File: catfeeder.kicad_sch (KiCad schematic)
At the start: 81 parts, among them J1 Barrel_Jack_Switch, J2 USB_B_Mini, J3 RFID, J4 DoorOpen, J5 Scale, J6 Auger Motor, J7 Door Motor, J8 DoorClose, Q1 UMH3N, Q3 MMBT4403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

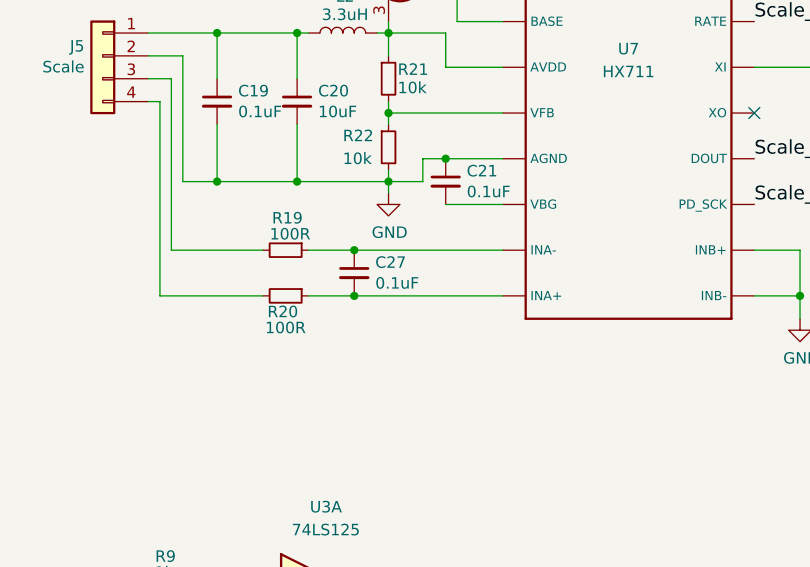
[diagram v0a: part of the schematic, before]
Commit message: Save with new KiCAD version. Cleanup some tracks and vias.
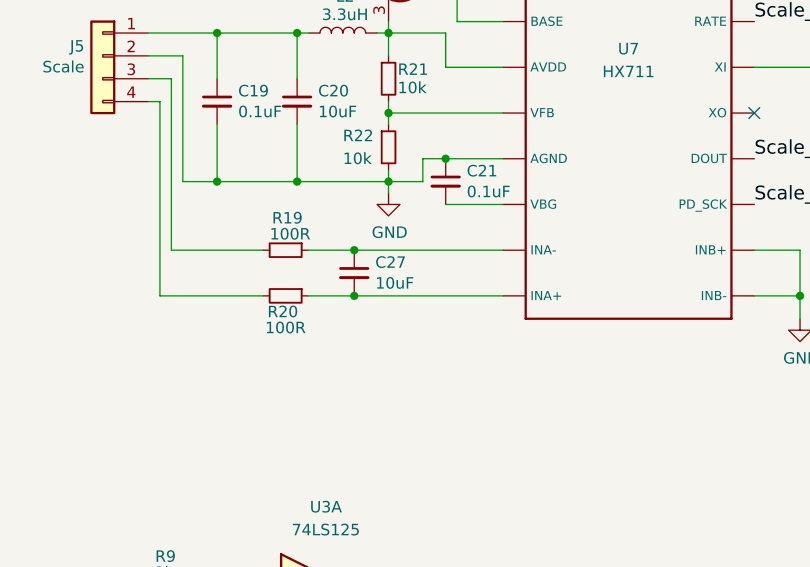
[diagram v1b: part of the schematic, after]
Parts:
- C27: value 0.1uF -> 10uF
